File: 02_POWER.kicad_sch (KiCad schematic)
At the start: 20 parts, among them U1 nPM1300-QEXX

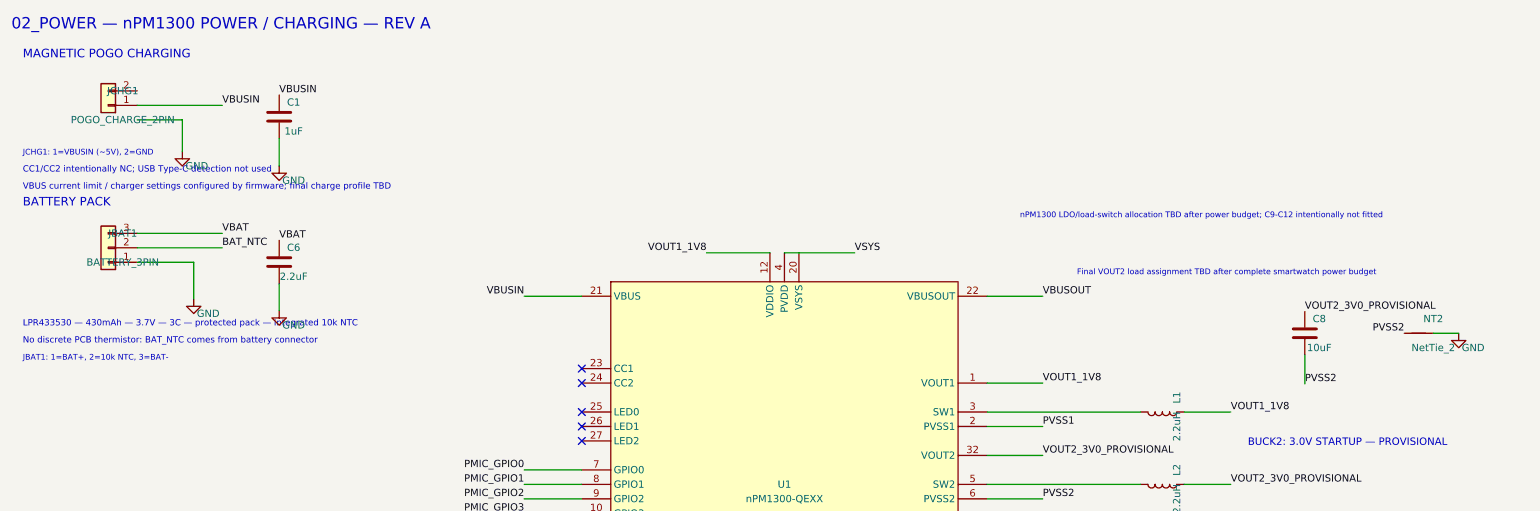
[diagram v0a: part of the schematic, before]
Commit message: updated schematics
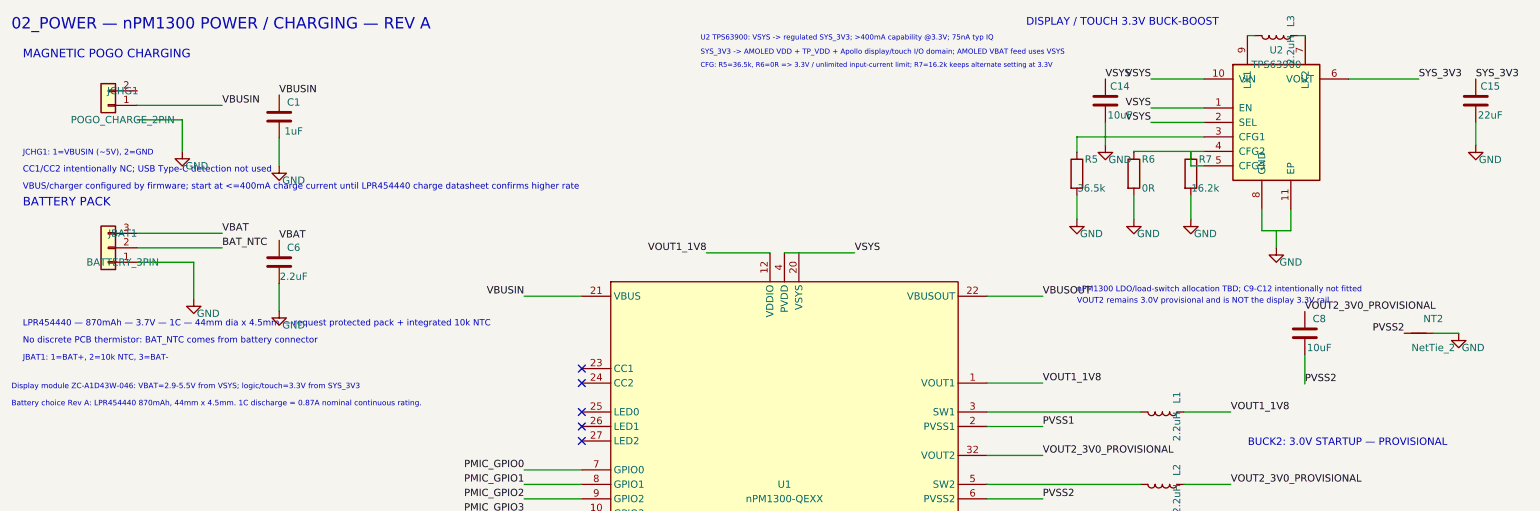
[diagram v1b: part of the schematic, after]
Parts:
- added C14: 10uF, Capacitor_SMD:C_0603_1608Metric, symbol Device:C
- added C15: 22uF, Capacitor_SMD:C_0603_1608Metric, symbol Device:C
- added L3: 2.2uH, symbol Device:L
- added R5: 36.5k, Resistor_SMD:R_0402_1005Metric, symbol Device:R
- added R6: 0R, Resistor_SMD:R_0402_1005Metric, symbol Device:R
- added R7: 16.2k, Resistor_SMD:R_0402_1005Metric, symbol Device:R
- added U2: TPS63900, Package_SON:WSON-10-1EP_2.5x2.5mm_P0.5mm_EP1.2x2mm_ThermalVias, symbol Regulator_Switching:TPS63900
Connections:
- net GND: now also C14.2, C15.2, R5.2, R6.2, R7.2
- net VSYS: now also C14.1, U2.1 (EN), U2.10 (VIN), U2.2 (SEL)
- new net: R6.1, U2.4 (CFG2)
- new net: L3.1, U2.7 (LX2)
- new net: L3.2, U2.9 (LX1)
- new net: R5.1, U2.3 (CFG1)
- new net: U2.11 (EP), U2.8 (GND)
- new net: R7.1, U2.5 (CFG3)
- new net SYS_3V3: C15.1, U2.6 (VOUT)
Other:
- note added: "Battery choice Rev A: LPR454440 870mAh, 44mm x 4.5mm. 1C discharge = 0.87A nominal continuous rating."
- note added: "CFG: R5=36.5k, R6=0R => 3.3V / unlimited input-current limit; R7=16.2k keeps alternate setting at 3.3V"
- note added: "DISPLAY / TOUCH 3.3V BUCK-BOOST"
- note added: "Display module ZC-A1D43W-046: VBAT=2.9-5.5V from VSYS; logic/touch=3.3V from SYS_3V3"
- note added: "LPR454440 — 870mAh — 3.7V — 1C — 44mm dia x 4.5mm — request protected pack + integrated 10k NTC"
- note added: "SYS_3V3 -> AMOLED VDD + TP_VDD + Apollo display/touch I/O domain; AMOLED VBAT feed uses VSYS"
- note added: "U2 TPS63900: VSYS -> regulated SYS_3V3; >400mA capability @3.3V; 75nA typ IQ"
- note added: "VBUS/charger configured by firmware; start at <=400mA charge current until LPR454440 charge datasheet confirms higher rate"
- note added: "VOUT2 remains 3.0V provisional and is NOT the display 3.3V rail"
- note added: "nPM1300 LDO/load-switch allocation TBD; C9-C12 intentionally not fitted"
- note removed: "Final VOUT2 load assignment TBD after complete smartwatch power budget"
- note removed: "LPR433530 — 430mAh — 3.7V — 3C — protected pack — integrated 10k NTC"
- note removed: "VBUS current limit / charger settings configured by firmware; final charge profile TBD"
- note removed: "nPM1300 LDO/load-switch allocation TBD after power budget; C9-C12 intentionally not fitted"

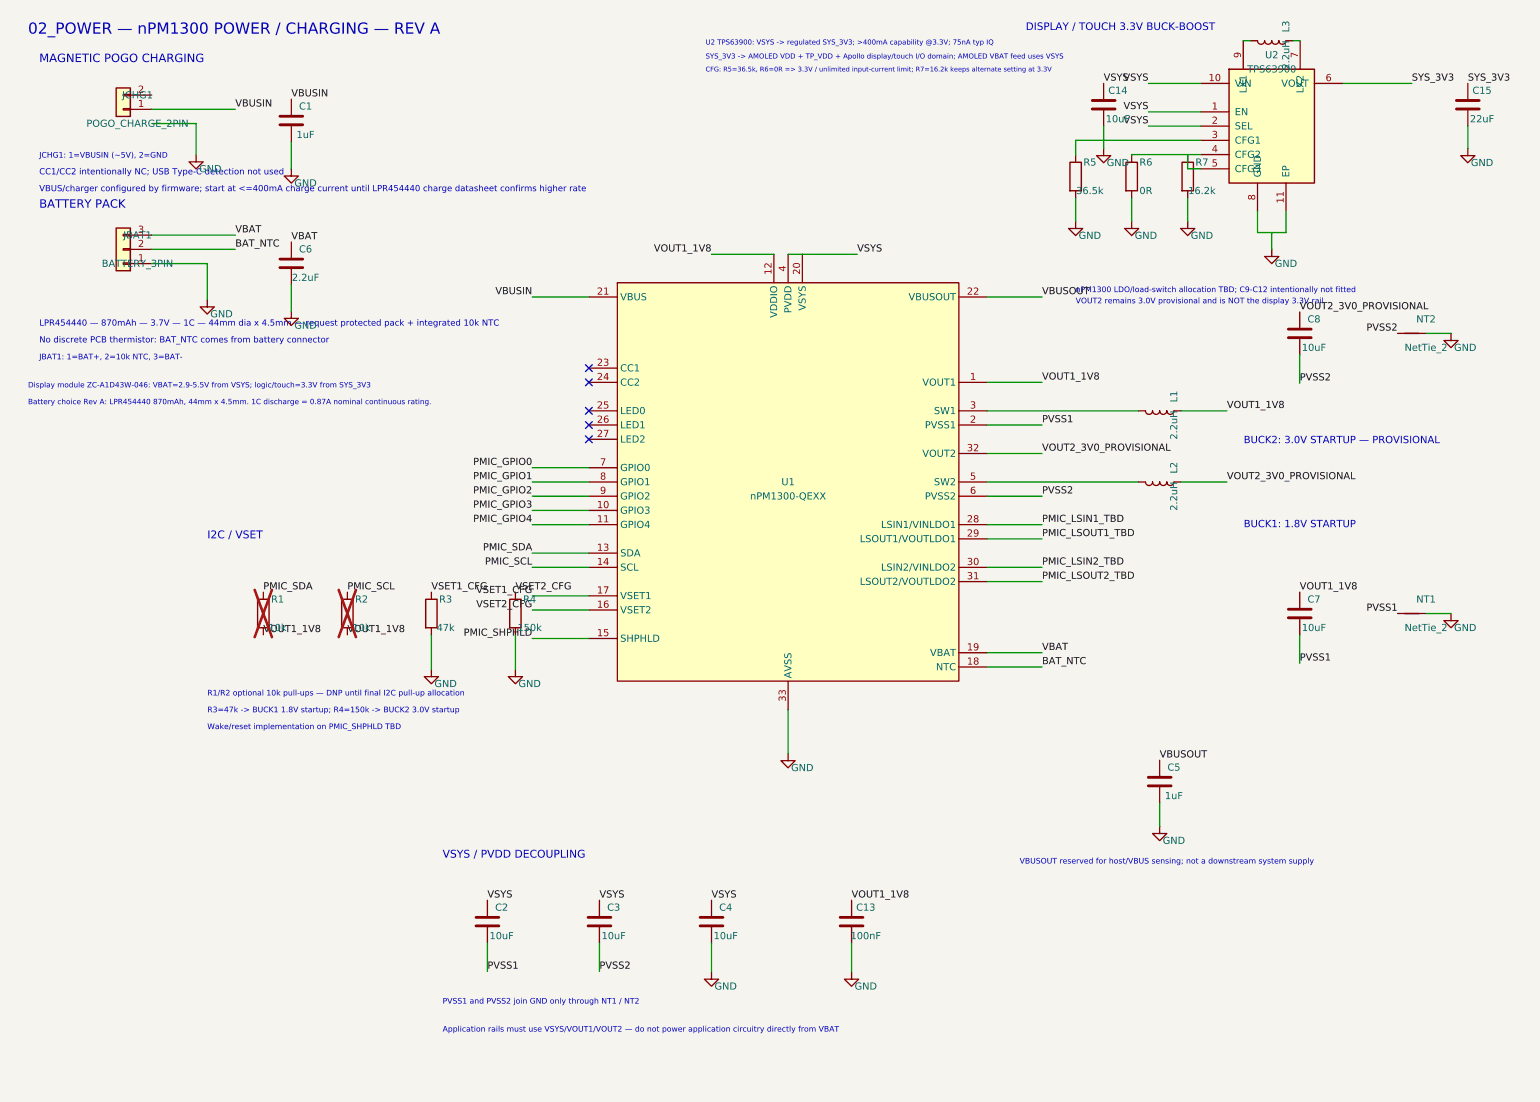
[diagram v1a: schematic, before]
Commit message: fixed schematics errors
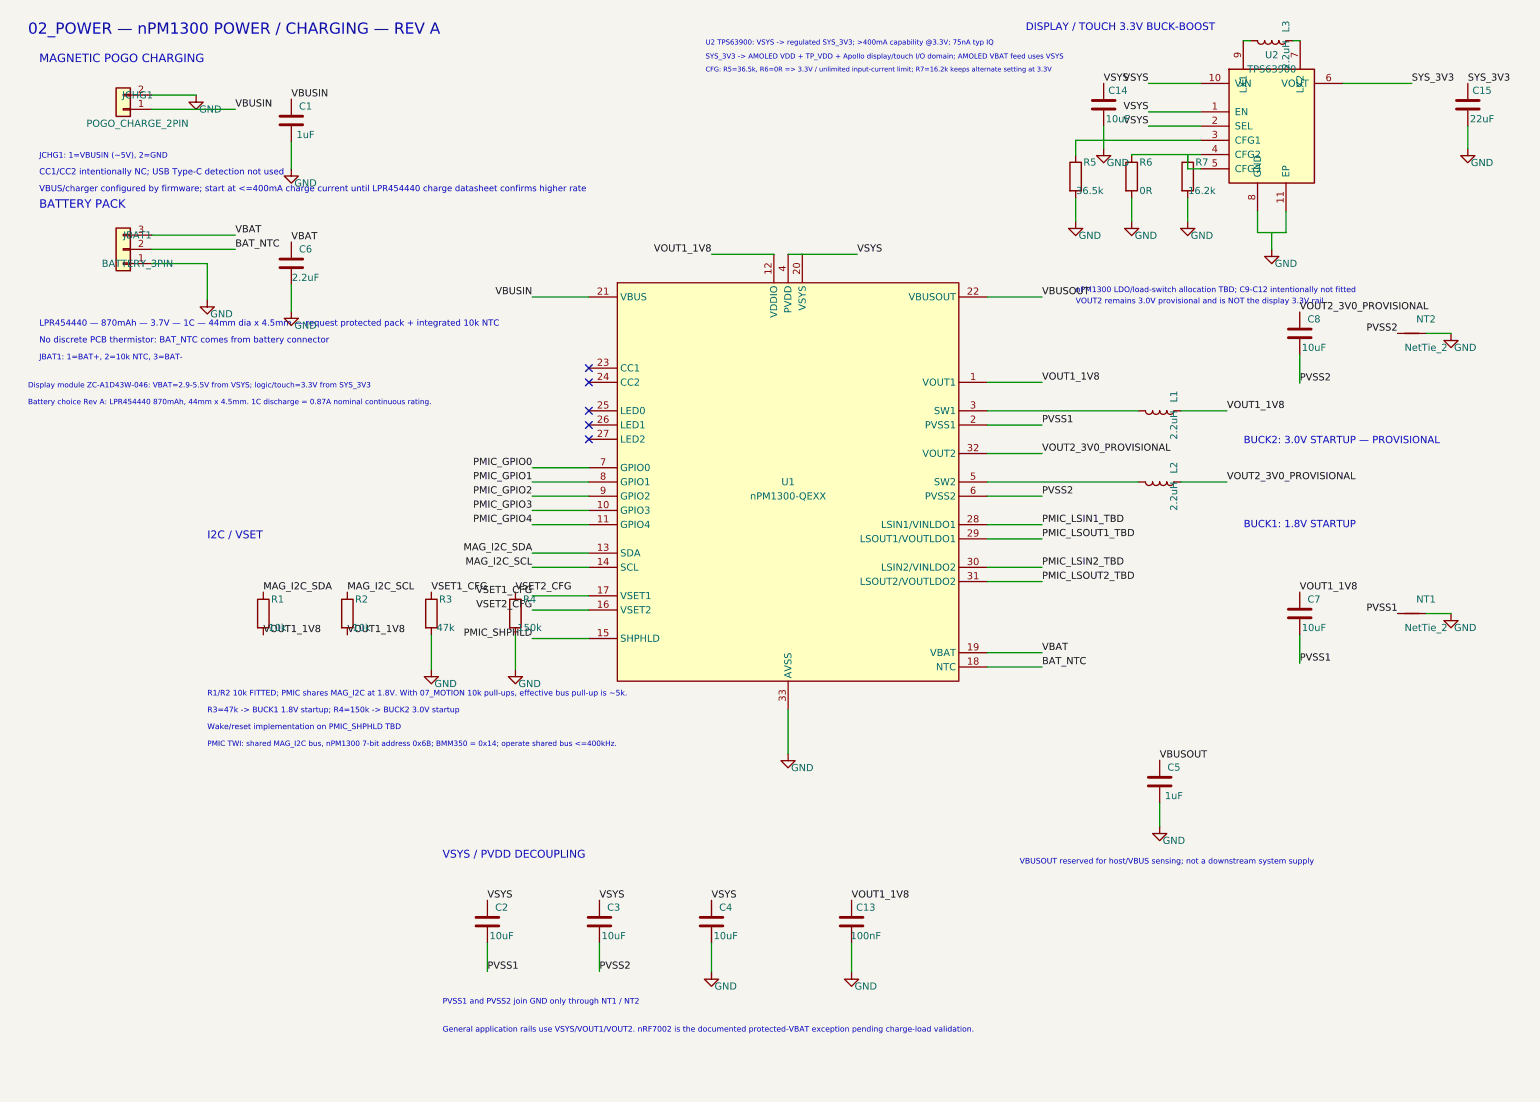
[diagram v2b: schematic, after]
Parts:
- R1, R2: Assembly DNP / optional -> FIT; now fitted
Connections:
- net GND: now also JCHG1.2 (Pin_2), U2.11 (EP), U2.8 (GND)
- net PMIC_SCL renamed MAG_I2C_SCL
- net PMIC_SDA renamed MAG_I2C_SDA
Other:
- note added: "General application rails use VSYS/VOUT1/VOUT2. nRF7002 is the documented protected-VBAT exception pending charge-load validation."
- note added: "PMIC TWI: shared MAG_I2C bus, nPM1300 7-bit address 0x6B; BMM350 = 0x14; operate shared bus <=400kHz."
- note added: "R1/R2 10k FITTED; PMIC shares MAG_I2C at 1.8V. With 07_MOTION 10k pull-ups, effective bus pull-up is ~5k."
- note removed: "Application rails must use VSYS/VOUT1/VOUT2 — do not power application circuitry directly from VBAT"
- note removed: "R1/R2 optional 10k pull-ups — DNP until final I2C pull-up allocation"
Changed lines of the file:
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@@
 		)
 	)
-	(text "R1/R2 optional 10k pull-ups — DNP until final I2C pull-up allocation"
+	(text "R1/R2 10k FITTED; PMIC shares MAG_I2C at 1.8V. With 07_MOTION 10k pull-ups, effective bus pull-up is ~5k."
 		(exclude_from_sim no)
 		(at 50 135 0)
@@
 		)
 	)
-	(text "Application rails must use VSYS/VOUT1/VOUT2 — do not power application circuitry directly from VBAT"
+	(text "General application rails use VSYS/VOUT1/VOUT2. nRF7002 is the documented protected-VBAT exception pending charge-load validation."
 		(exclude_from_sim no)
 		(at 92 195 0)
@@
 		)
 	)
+	(text "PMIC TWI: shared MAG_I2C bus, nPM1300 7-bit address 0x6B; BMM350 = 0x14; operate shared bus <=400kHz."
+		(exclude_from_sim no)
+		(at 50 144 0)
+		(effects
+			(font
+				(size 0.95 0.95)
+			)
+			(justify left bottom)
+		)
+	)
 	(no_connect
 		(at 118.11 78.74)
@@
 	(wire
 		(pts
-			(xy 237.46 52) (xy 242.54 52)
-		)
-		(stroke
-			(width 0)
-			(type default)
-		)
-	)
-	(wire
-		(pts
-			(xy 40.08 57.54) (xy 50 57.54)
+			(xy 237.46 52) (xy 240 52)
 		)
 		(stroke
@@
 	(wire
 		(pts
-			(xy 40.08 32.54) (xy 48 32.54)
+			(xy 240 52) (xy 242.54 52)
 		)
 		(stroke
@@
 	(wire
 		(pts
-			(xy 48 32.54) (xy 48 38.1)
+			(xy 40.08 57.54) (xy 50 57.54)
 		)
 		(stroke
@@
 		)
 	)
-	(label "PMIC_SCL"
+	(label "MAG_I2C_SCL"
 		(at 108 111.76 180)
 		(effects
@@
 		)
 	)
-	(label "PMIC_SCL"
+	(label "MAG_I2C_SCL"
 		(at 75 116.19 0)
 		(effects
@@
 		)
 	)
-	(label "PMIC_SDA"
+	(label "MAG_I2C_SDA"
 		(at 60 116.19 0)
 		(effects
@@
 		)
 	)
-	(label "PMIC_SDA"
+	(label "MAG_I2C_SDA"
 		(at 108 109.22 180)
 		(effects
@@
 		)
 	)
+	(wire
+		(pts
+			(xy 40.08 27.46) (xy 48 27.46)
+		)
+		(stroke
+			(width 0)
+			(type default)
+		)
+	)
 	(symbol
 		(lib_id "Device:C")
@@
 	(symbol
 		(lib_id "power:GND")
-		(at 48 38.1 0)
+		(at 48 27.46 0)
 		(unit 1)
 		(body_style 1)
@@
 		(fields_autoplaced yes)
 		(property "Reference" "#PWR001"
-			(at 50.54 35.56 0)
+			(at 50.54 24.92 0)
 			(hide yes)
 			(show_name no)
@@
 		)
 		(property "Value" "GND"
-			(at 50.54 40.64 0)
+			(at 50.54 30 0)
 			(show_name no)
 			(do_not_autoplace no)
@@
 		)
 		(property "Footprint" ""
-			(at 48 38.1 0)
+			(at 48 27.46 0)
 			(hide yes)
 			(show_name no)
@@
 		)
 		(property "Datasheet" "~"
-			(at 48 38.1 0)
+			(at 48 27.46 0)
 			(hide yes)
 			(show_name no)
@@
 		)
 		(property "Description" "Power symbol creates a global label with name GND"
-			(at 48 38.1 0)
+			(at 48 27.46 0)
 			(hide yes)
 			(show_name no)
@@
 		(on_board yes)
 		(in_pos_files yes)
-		(dnp yes)
+		(dnp no)
 		(fields_autoplaced yes)
 		(property "Reference" "R1"
@@
 			)
 		)
-		(property "Description" "Optional PMIC SDA pull-up; DNP"
+		(property "Description" "Fitted 10k pull-up for shared nPM1300/BMM350 1.8V I2C bus"
 			(at 60 120 0)
 			(hide yes)
@@
 			)
 		)
-		(property "Assembly" "DNP / optional"
+		(property "Assembly" "FIT"
 			(at 60 120 0)
 			(hide yes)
@@
 		(on_board yes)
 		(in_pos_files yes)
-		(dnp yes)
+		(dnp no)
 		(fields_autoplaced yes)
 		(property "Reference" "R2"
@@
 			)
 		)
-		(property "Description" "Optional PMIC SCL pull-up; DNP"
+		(property "Description" "Fitted 10k pull-up for shared nPM1300/BMM350 1.8V I2C bus"
 			(at 75 120 0)
 			(hide yes)
@@
 			)
 		)
-		(property "Assembly" "DNP / optional"
+		(property "Assembly" "FIT"
 			(at 75 120 0)
 			(hide yes)

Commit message: refactor(kicad): integrate Rev-A hierarchy and libraries
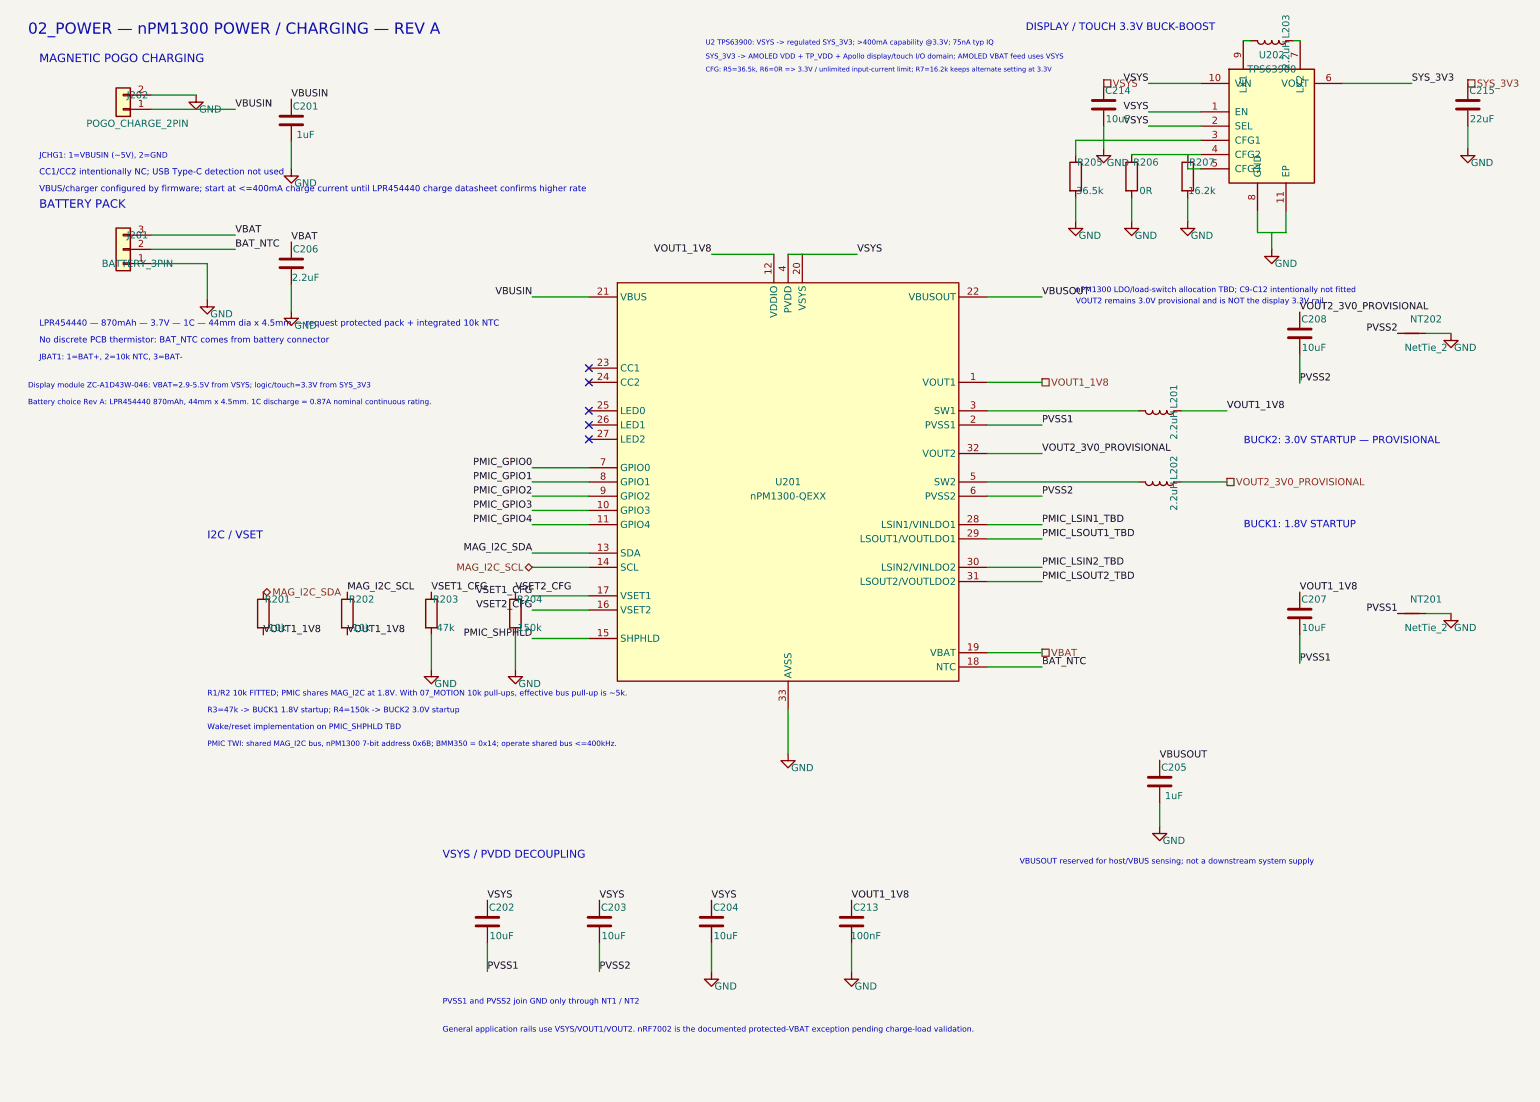
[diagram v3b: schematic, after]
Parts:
- renumbered C1 to C201, C2 to C202, C3 to C203, C4 to C204, C5 to C205, C6 to C206, C7 to C207, C8 to C208, C13 to C213, C14 to C214, C15 to C215, JBAT1 to J201, JCHG1 to J202, L1 to L201, L2 to L202, L3 to L203, NT1 to NT201, NT2 to NT202, R1 to R201, R2 to R202, R3 to R203, R4 to R204, R5 to R205, R6 to R206, R7 to R207, U1 to U201, U2 to U202
